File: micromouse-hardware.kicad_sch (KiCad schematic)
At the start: 52 parts, among them Q1 MBT3904DW1, Q2 MBT3904DW1, Q3 MBT3904DW1, Q4 TEFT4300, Q5 TEFT4300, Q6 TEFT4300, Q7 TEFT4300, Q8 TEFT4300, SW1 SLW-116641-5A-S-D, SW2 SW_DIP_x02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

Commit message: before routing
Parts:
- BT1: footprint (none) -> Connector_PinHeader_2.54mm:PinHeader_1x02_P2.54mm_Vertical
- C1, C2, C3, C4, C5: footprint Capacitor_SMD:C_0201_0603Metric -> Capacitor_SMD:C_0603_1608Metric
- L1: value 220uH -> 22uH; footprint Inductor_SMD:L_0201_0603Metric -> Inductor_SMD:L_7.3x7.3_H3.5
- R1, R10, R11, R12, R13, R14, R15, R2, R21, R22, R3, R4, R5, R6, R7, R8, R9: footprint Resistor_SMD:R_0201_0603Metric -> Resistor_SMD:R_0603_1608Metric
- U2: value 74HC4051 -> CD74HC4051NSR; footprint Package_SO:SOIC-14-16_3.9x9.9mm_P1.27mm -> Package_SO:SOIC-16_4.55x10.3mm_P1.27mm
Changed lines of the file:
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@@
 	(label "D11"
 		(at 191.77 203.2 180)
+		(fields_autoplaced yes)
 		(effects
 			(font
@@
 	(label "MUX_SEL_0"
 		(at 95.25 129.54 270)
+		(fields_autoplaced yes)
 		(effects
 			(font
@@
 	(label "D5"
 		(at 190.5 195.58 180)
+		(fields_autoplaced yes)
 		(effects
 			(font
@@
 	(label "A0"
 		(at 261.62 181.61 180)
+		(fields_autoplaced yes)
 		(effects
 			(font
@@
 	(label "D11"
 		(at 90.17 203.2 180)
+		(fields_autoplaced yes)
 		(effects
 			(font
@@
 	(label "IRT_READ"
 		(at 295.91 101.6 180)
+		(fields_autoplaced yes)
 		(effects
 			(font
@@
 	(label "IRT_READ"
 		(at 118.11 190.5 0)
+		(fields_autoplaced yes)
 		(effects
 			(font
@@
 	(label "MUX_SEL_0"
 		(at 300.99 101.6 270)
+		(fields_autoplaced yes)
 		(effects
 			(font
@@
 	(label "D5"
 		(at 88.9 187.96 180)
+		(fields_autoplaced yes)
 		(effects
 			(font
@@
 	(label "A1"
 		(at 261.62 184.15 180)
+		(fields_autoplaced yes)
 		(effects
 			(font
@@
 	(label "D3"
 		(at 190.5 200.66 180)
+		(fields_autoplaced yes)
 		(effects
 			(font
@@
 	(label "D6"
 		(at 88.9 190.5 180)
+		(fields_autoplaced yes)
 		(effects
 			(font
@@
 	(label "A2"
 		(at 261.62 203.2 180)
+		(fields_autoplaced yes)
 		(effects
 			(font
@@
 	(label "MUX_SEL_1"
 		(at 303.53 101.6 270)
+		(fields_autoplaced yes)
 		(effects
 			(font
@@
 	(label "MUX_SEL_0"
 		(at 92.71 185.42 180)
+		(fields_autoplaced yes)
 		(effects
 			(font
@@
 	(label "MUX_SEL_1"
 		(at 97.79 129.54 270)
+		(fields_autoplaced yes)
 		(effects
 			(font
@@
 	(label "MUX_SEL_1"
 		(at 92.71 193.04 180)
+		(fields_autoplaced yes)
 		(effects
 			(font
@@
 	(label "LED_DEMUX_ENABLE"
 		(at 92.71 180.34 180)
+		(fields_autoplaced yes)
 		(effects
 			(font
@@
 	(label "LED_DEMUX_ENABLE"
 		(at 113.03 129.54 0)
+		(fields_autoplaced yes)
 		(effects
 			(font
@@
 	(label "A3"
 		(at 261.62 205.74 180)
+		(fields_autoplaced yes)
 		(effects
 			(font
@@
 	(label "MUX_SEL_2"
 		(at 92.71 195.58 180)
+		(fields_autoplaced yes)
 		(effects
 			(font
@@
 	(label "MUX_SEL_2"
 		(at 100.33 129.54 270)
+		(fields_autoplaced yes)
 		(effects
 			(font
@@
 	(label "D3"
 		(at 88.9 182.88 180)
+		(fields_autoplaced yes)
 		(effects
 			(font
@@
 	(label "D6"
 		(at 190.5 198.12 180)
+		(fields_autoplaced yes)
 		(effects
 			(font
@@
 	(label "MUX_SEL_2"
 		(at 306.07 101.6 270)
+		(fields_autoplaced yes)
 		(effects
 			(font
@@
 			)
 		)
-		(property "Footprint" "Resistor_SMD:R_0201_0603Metric"
+		(property "Footprint" "Resistor_SMD:R_0603_1608Metric"
 			(at 214.122 46.99 90)
 			(effects
@@
 			)
 		)
-		(property "Footprint" "Resistor_SMD:R_0201_0603Metric"
+		(property "Footprint" "Resistor_SMD:R_0603_1608Metric"
 			(at 203.2 61.468 90)
 			(effects
@@
 			)
 		)
-		(property "Footprint" "Resistor_SMD:R_0201_0603Metric"
+		(property "Footprint" "Resistor_SMD:R_0603_1608Metric"
 			(at 85.09 72.898 90)
 			(effects
@@
 			)
 		)
-		(property "Footprint" "Resistor_SMD:R_0201_0603Metric"
+		(property "Footprint" "Resistor_SMD:R_0603_1608Metric"
 			(at 46.99 72.898 90)
 			(effects
@@
 			)
 		)
-		(property "Footprint" "Resistor_SMD:R_0201_0603Metric"
+		(property "Footprint" "Resistor_SMD:R_0603_1608Metric"
 			(at 41.91 61.468 90)
 			(effects
@@
 			)
 		)
-		(property "Value" "74HC4051"
+		(property "Value" "CD74HC4051NSR"
 			(at 287.02 91.0238 90)
 			(effects
@@
 			)
 		)
-		(property "Footprint" "Package_SO:SOIC-14-16_3.9x9.9mm_P1.27mm"
+		(property "Footprint" "Package_SO:SOIC-16_4.55x10.3mm_P1.27mm"
 			(at 313.69 93.98 0)
 			(effects
@@
 			)
 		)
-		(property "Footprint" "Resistor_SMD:R_0201_0603Metric"
+		(property "Footprint" "Resistor_SMD:R_0603_1608Metric"
 			(at 119.38 61.468 90)
 			(effects
@@
 			)
 		)
-		(property "Footprint" ""
+		(property "Footprint" "Connector_PinHeader_2.54mm:PinHeader_1x02_P2.54mm_Vertical"
 			(at 306.07 180.086 90)
 			(effects
@@
 			)
 		)
-		(property "Footprint" "Resistor_SMD:R_0201_0603Metric"
+		(property "Footprint" "Resistor_SMD:R_0603_1608Metric"
 			(at 375.412 181.61 90)
 			(effects
@@
 			)
 		)
-		(property "Footprint" "Capacitor_SMD:C_0201_0603Metric"
+		(property "Footprint" "Capacitor_SMD:C_0603_1608Metric"
 			(at 328.6252 181.61 0)
 			(effects
@@
 			)
 		)
-		(property "Footprint" "Capacitor_SMD:C_0201_0603Metric"
+		(property "Footprint" "Capacitor_SMD:C_0603_1608Metric"
 			(at 390.8552 187.96 0)
 			(effects
@@
 			)
 		)
-		(property "Footprint" "Capacitor_SMD:C_0201_0603Metric"
+		(property "Footprint" "Capacitor_SMD:C_0603_1608Metric"
 			(at 183.8452 180.34 0)
 			(effects
@@
 			)
 		)
-		(property "Footprint" "Resistor_SMD:R_0201_0603Metric"
+		(property "Footprint" "Resistor_SMD:R_0603_1608Metric"
 			(at 124.46 72.898 90)
 			(effects
@@
 			)
 		)
-		(property "Footprint" "Resistor_SMD:R_0201_0603Metric"
+		(property "Footprint" "Resistor_SMD:R_0603_1608Metric"
 			(at 208.28 72.898 90)
 			(effects
@@
 			)
 		)
-		(property "Value" "220uH"
+		(property "Value" "22uH"
 			(at 351.79 171.45 90)
 			(effects
@@
 			)
 		)
-		(property "Footprint" "Inductor_SMD:L_0201_0603Metric"
+		(property "Footprint" "Inductor_SMD:L_7.3x7.3_H3.5"
 			(at 351.79 173.99 0)
 			(effects
@@
 			)
 		)
-		(property "Description" "Inductor"
+		(property "Description" "IFDC3030EZER220M"
 			(at 351.79 173.99 0)
 			(effects
@@
 			)
 		)
-		(property "Footprint" "Capacitor_SMD:C_0201_0603Metric"
+		(property "Footprint" "Capacitor_SMD:C_0603_1608Metric"
 			(at 224.4852 179.07 0)
 			(effects
@@
 			)
 		)
-		(property "Footprint" "Resistor_SMD:R_0201_0603Metric"
+		(property "Footprint" "Resistor_SMD:R_0603_1608Metric"
 			(at 168.402 46.99 90)
 			(effects
@@
 			)
 		)
-		(property "Footprint" "Resistor_SMD:R_0201_0603Metric"
+		(property "Footprint" "Resistor_SMD:R_0603_1608Metric"
 			(at 157.48 61.468 90)
 			(effects
@@
 			)
 		)
-		(property "Footprint" "Resistor_SMD:R_0201_0603Metric"
+		(property "Footprint" "Resistor_SMD:R_0603_1608Metric"
 			(at 80.01 61.468 90)
 			(effects
@@
 			)
 		)
-		(property "Footprint" "Resistor_SMD:R_0201_0603Metric"
+		(property "Footprint" "Resistor_SMD:R_0603_1608Metric"
 			(at 52.832 46.99 90)
 			(effects
@@
 			)
 		)
-		(property "Footprint" "Resistor_SMD:R_0201_0603Metric"
+		(property "Footprint" "Resistor_SMD:R_0603_1608Metric"
 			(at 90.932 46.99 90)
 			(effects
@@
 			)
 		)
-		(property "Footprint" "Capacitor_SMD:C_0201_0603Metric"
+		(property "Footprint" "Capacitor_SMD:C_0603_1608Metric"
 			(at 233.3752 179.07 0)
 			(effects
@@
 			)
 		)
-		(property "Footprint" "Resistor_SMD:R_0201_0603Metric"
+		(property "Footprint" "Resistor_SMD:R_0603_1608Metric"
 			(at 162.56 72.898 90)
 			(effects
@@
 			)
 		)
-		(property "Footprint" "Resistor_SMD:R_0201_0603Metric"
+		(property "Footprint" "Resistor_SMD:R_0603_1608Metric"
 			(at 130.302 46.99 90)
 			(effects
@@
 			)
 		)
-		(property "Footprint" "Resistor_SMD:R_0201_0603Metric"
+		(property "Footprint" "Resistor_SMD:R_0603_1608Metric"
 			(at 375.412 195.58 90)
 			(effects

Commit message: nesto stabilno
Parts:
- added R23, R24: 10K, Resistor_SMD:R_0603_1608Metric, symbol Device:R
- D6: footprint Diode_SMD:D_0201_0603Metric -> Diode_SMD:D_0603_1608Metric_Pad1.05x0.95mm_HandSolder
- U2: value CD74HC4051NSR -> CD74HC4051M
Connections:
- net GND: now also R23.1, R24.1
- net at A1.15 (D12), SW2.2: now also R24.2
- net at A1.16 (D13), SW2.1: now also R23.2

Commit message: before arduino rotae
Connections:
- net A0 is gone; now on net A1: ME1.3 (C1)
- net A1: now also A1.20 (A1); no longer ME1.4 (C2)
- net A2: now also A1.21 (A2), ME1.4 (C2); no longer ME2.3 (C1)
- net A3: now also A1.22 (A3)
- net A4: now reaches A1.23 (A4)
- net A4: now also ME2.3 (C1)
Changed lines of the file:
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@@
+	(wire
+		(pts
+			(xy 259.08 203.2) (xy 261.62 203.2)
+		)
+		(stroke
+			(width 0)
+			(type default)
+		)
+	)
 	(wire
 		(pts
@@
 		(pts
 			(xy 88.9 71.12) (xy 92.71 71.12)
+		)
+		(stroke
+			(width 0)
+			(type default)
+		)
+	)
+	(wire
+		(pts
+			(xy 259.08 205.74) (xy 261.62 205.74)
 		)
 		(stroke
@@
 		)
 	)
-	(label "A0"
+	(label "A3"
+		(at 118.11 198.12 0)
+		(effects
+			(font
+				(size 1.27 1.27)
+			)
+			(justify left bottom)
+		)
+	)
+	(label "A1"
 		(at 261.62 181.61 180)
 		(effects
@@
 		)
 	)
-	(label "A1"
+	(label "A4"
+		(at 259.08 203.2 0)
+		(effects
+			(font
+				(size 1.27 1.27)
+			)
+			(justify left bottom)
+		)
+	)
+	(label "A2"
 		(at 261.62 184.15 180)
 		(effects
@@
 			)
 			(justify right bottom)
+		)
+	)
+	(label "A2"
+		(at 118.11 195.58 0)
+		(effects
+			(font
+				(size 1.27 1.27)
+			)
+			(justify left bottom)
 		)
 	)
@@
 		)
 	)
-	(label "A2"
-		(at 261.62 203.2 180)
-		(effects
-			(font
-				(size 1.27 1.27)
-			)
-			(justify right bottom)
-		)
-	)
 	(label "MUX_SEL_1"
 		(at 303.53 101.6 270)
@@
 		)
 	)
-	(label "A3"
-		(at 261.62 205.74 180)
-		(effects
-			(font
-				(size 1.27 1.27)
-			)
-			(justify right bottom)
+	(label "A4"
+		(at 118.11 200.66 0)
+		(effects
+			(font
+				(size 1.27 1.27)
+			)
+			(justify left bottom)
+		)
+	)
+	(label "A1"
+		(at 118.11 193.04 0)
+		(effects
+			(font
+				(size 1.27 1.27)
+			)
+			(justify left bottom)
 		)
 	)
@@
 		)
 	)
+	(label "A3"
+		(at 259.08 205.74 0)
+		(effects
+			(font
+				(size 1.27 1.27)
+			)
+			(justify left bottom)
+		)
+	)

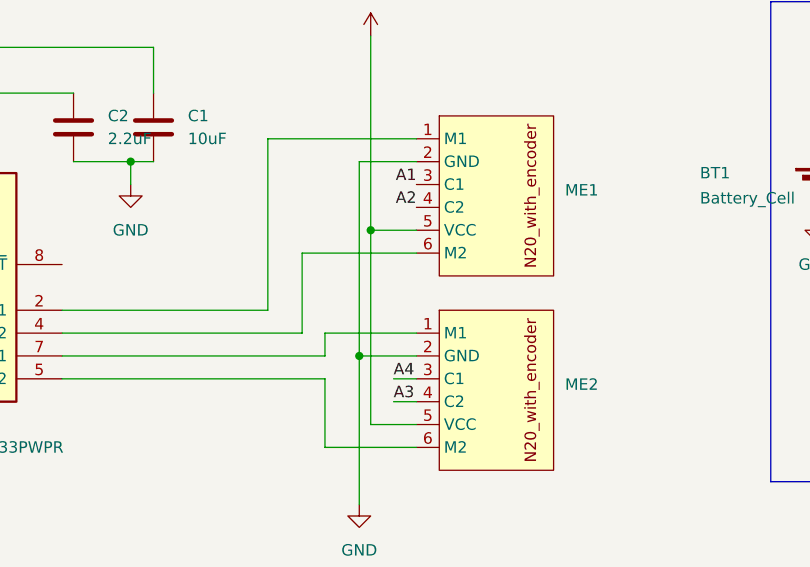
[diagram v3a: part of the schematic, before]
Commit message: everything except ground plane
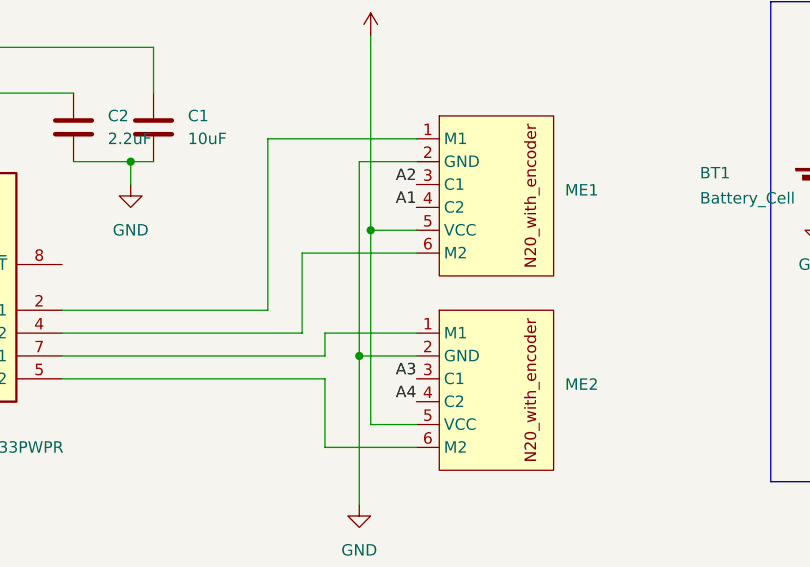
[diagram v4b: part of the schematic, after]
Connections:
- net A1: now also ME1.4 (C2); no longer ME1.3 (C1)
- net A2: now also ME1.3 (C1); no longer ME1.4 (C2)
- net A3: now also ME2.3 (C1); no longer ME2.4 (C2)
- net A4: now also ME2.4 (C2); no longer ME2.3 (C1)
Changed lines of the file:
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@@
-	(wire
-		(pts
-			(xy 259.08 203.2) (xy 261.62 203.2)
-		)
-		(stroke
-			(width 0)
-			(type default)
-		)
-	)
 	(wire
 		(pts
@@
 		(pts
 			(xy 88.9 71.12) (xy 92.71 71.12)
-		)
-		(stroke
-			(width 0)
-			(type default)
-		)
-	)
-	(wire
-		(pts
-			(xy 259.08 205.74) (xy 261.62 205.74)
 		)
 		(stroke
@@
 	)
 	(label "A1"
-		(at 261.62 181.61 180)
+		(at 261.62 184.15 180)
 		(effects
 			(font
@@
 		)
 	)
-	(label "A4"
-		(at 259.08 203.2 0)
-		(effects
-			(font
-				(size 1.27 1.27)
-			)
-			(justify left bottom)
-		)
-	)
 	(label "A2"
-		(at 261.62 184.15 180)
+		(at 261.62 181.61 180)
 		(effects
 			(font
@@
 		)
 	)
+	(label "A3"
+		(at 261.62 203.2 180)
+		(effects
+			(font
+				(size 1.27 1.27)
+			)
+			(justify right bottom)
+		)
+	)
 	(label "MUX_SEL_1"
 		(at 303.53 101.6 270)
@@
 		)
 	)
+	(label "A4"
+		(at 261.62 205.74 180)
+		(effects
+			(font
+				(size 1.27 1.27)
+			)
+			(justify right bottom)
+		)
+	)
 	(label "MUX_SEL_2"
 		(at 92.71 195.58 180)
@@
 		)
 	)
-	(label "A3"
-		(at 259.08 205.74 0)
-		(effects
-			(font
-				(size 1.27 1.27)
-			)
-			(justify left bottom)
-		)
-	)

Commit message: limit
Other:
- note added: "5V regulator - peak ~1A i const ~300mA"
- note removed: "5V regulator"
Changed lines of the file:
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@@
 		)
 	)
-	(text "5V regulator"
+	(text "5V regulator - peak ~1A i const ~300mA"
 		(exclude_from_sim no)
-		(at 307.848 159.258 0)
+		(at 321.31 159.004 0)
 		(effects
 			(font

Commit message: Arduino Nano - Regulated 5V should be connected to 5V not VIN Moved some labels around to make connections more visible Placed No Connect Flags on all unused pins Added descriptive names to labels Changed the 5V regulator to LM2575GR-5.0 Made the Motor Driver use the battery voltage directly Re-routed some parts of the PCB to make space
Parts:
- removed D6: SS34, Diode_SMD:D_0603_1608Metric_Pad1.05x0.95mm_HandSolder, symbol Device:D_Schottky
- removed R21: 110K, Resistor_SMD:R_0603_1608Metric, symbol Device:R
- removed R22: 15K, Resistor_SMD:R_0603_1608Metric, symbol Device:R
- removed SW1: SLW-116641-5A-S-D, Connector_PinHeader_2.54mm:PinHeader_1x03_P2.54mm_Vertical, symbol Switch:SW_SPDT
- removed U4: MT3608, Package_TO_SOT_SMD:SOT-23-6, symbol Regulator_Switching:MT3608
- added BT2: Battery_Cell, Connector_PinHeader_2.54mm:PinHeader_1x02_P2.54mm_Vertical, symbol Device:Battery_Cell
- added C6: 470uF, Capacitor_SMD:C_Elec_8x10.2, symbol Device:C
- added C7: 100nF, Capacitor_SMD:C_0603_1608Metric, symbol Device:C
- added D8: SS26, Diode_SMD:D_SMA, symbol Diode:SS26
- added J1: BATT-CONN, Connector_PinHeader_2.54mm:PinHeader_1x02_P2.54mm_Vertical, symbol Connector_Generic:Conn_01x02
- added unit 2 of Q3
- added SW3: SLW-116641-5A-S-D, Connector_PinHeader_2.54mm:PinHeader_1x03_P2.54mm_Vertical, symbol Switch:SW_SPDT
- added U5: LM2575GR-5.0, Package_TO_SOT_SMD:TO-263-5_TabPin3, symbol Regulator_Switching:LM2575-5.0BU
- BT1: now left out of the parts list
- C4: value 22uF X7R -> 470uF; footprint Capacitor_SMD:C_0603_1608Metric -> Capacitor_SMD:C_Elec_8x10.2; Order Link (none) -> https://www.tme.eu/en/details/sc1c477m08010vr/smd-electroly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
- C5: value 22uF X7R -> 100nF; Order Link (none) -> https://www.tme.eu/en/details/cl10b104kb8nnnc/mlcc-smd-capa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
- L1: value 22uH -> 220uH; footprint Inductor_SMD:L_7.3x7.3_H3.5 -> Inductor_SMD:L_12x12mm_H8mm; Order Link (none) -> https://www.tme.eu/en/details/pcs129mt221/inductors/viking/
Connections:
- net +5V: now also A1.27 (+5V), C4.1, L1.2, C7.1, U5.4 (FB); no longer A1.30 (VIN), C1.1, C3.1, C5.1, U1.12 (VM)
- net GND: now also BT2.2 (-), C6.2, C7.2, D8.2 (A), J1.1 (Pin_1), Q3.3 (C2), Q3.4 (E2), Q3.5 (B2), U5.3 (GND), U5.5 (~{ON}/OFF); no longer BT1.2 (-)
- net at L1.1: now also D8.1 (K), U5.2 (OUT); no longer C4.1
- net at BT1.1 (+): now also J1.2 (Pin_2), SW3.2 (B)
- net A1 renamed M1-C1
- net M1-C1: now also ME1.3 (C1); no longer ME1.4 (C2)
- net A2 renamed M1-C2
- net M1-C2: now also ME1.4 (C2); no longer ME1.3 (C1)
- net A3 renamed M2-C1
- net M2-C1: now also A1.23 (A4); no longer A1.22 (A3)
- net A4 renamed M2-C2
- net M2-C2: now also A1.22 (A3); no longer A1.23 (A4)
- net D11 renamed M2-IN2
- net D3 renamed M2-IN1
- net D5 renamed M1-IN1
- net D6 renamed M1-IN2
- new net: BT1.2 (-), BT2.1 (+)
- new net +VBAT: C1.1, C3.1, C5.1, C6.1, SW3.1 (A), U1.12 (VM), U5.1 (VIN)
- no-connect marks 0 -> 20
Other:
- moved on the sheet: C3, ME1, ME2, R24

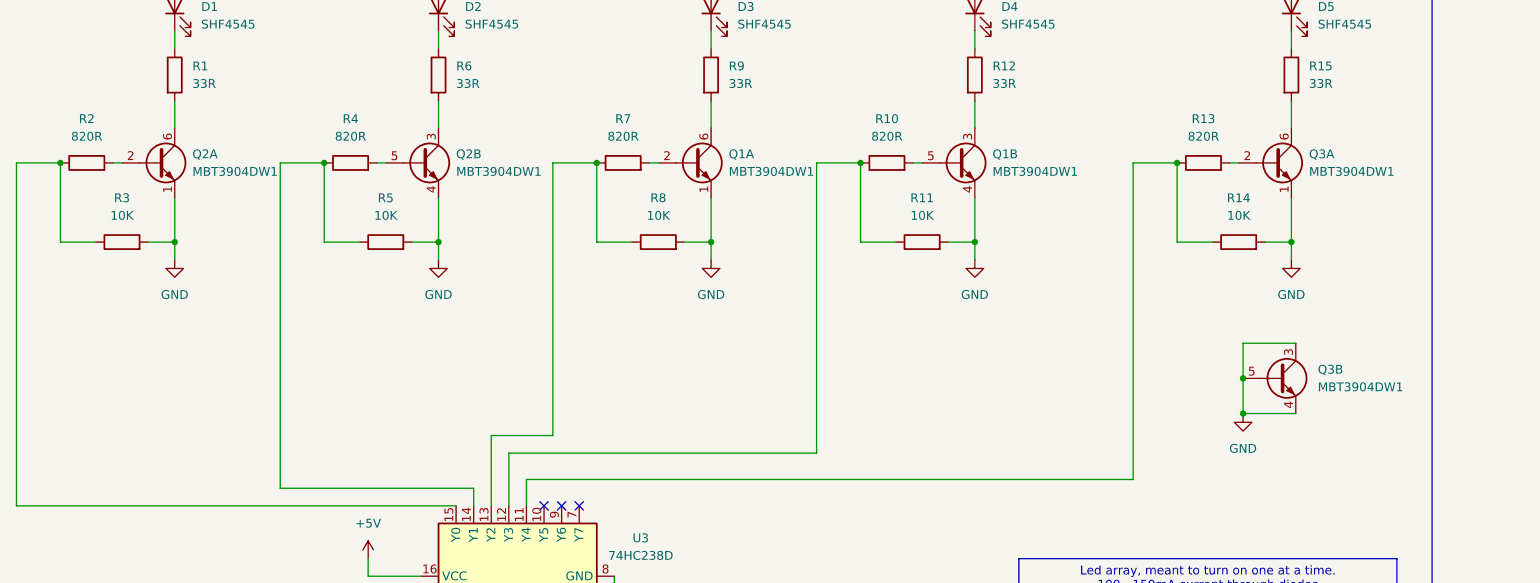
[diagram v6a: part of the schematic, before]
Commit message: Change the transistor footprint, changed spacing around the components to allow for mounting hardware to be added
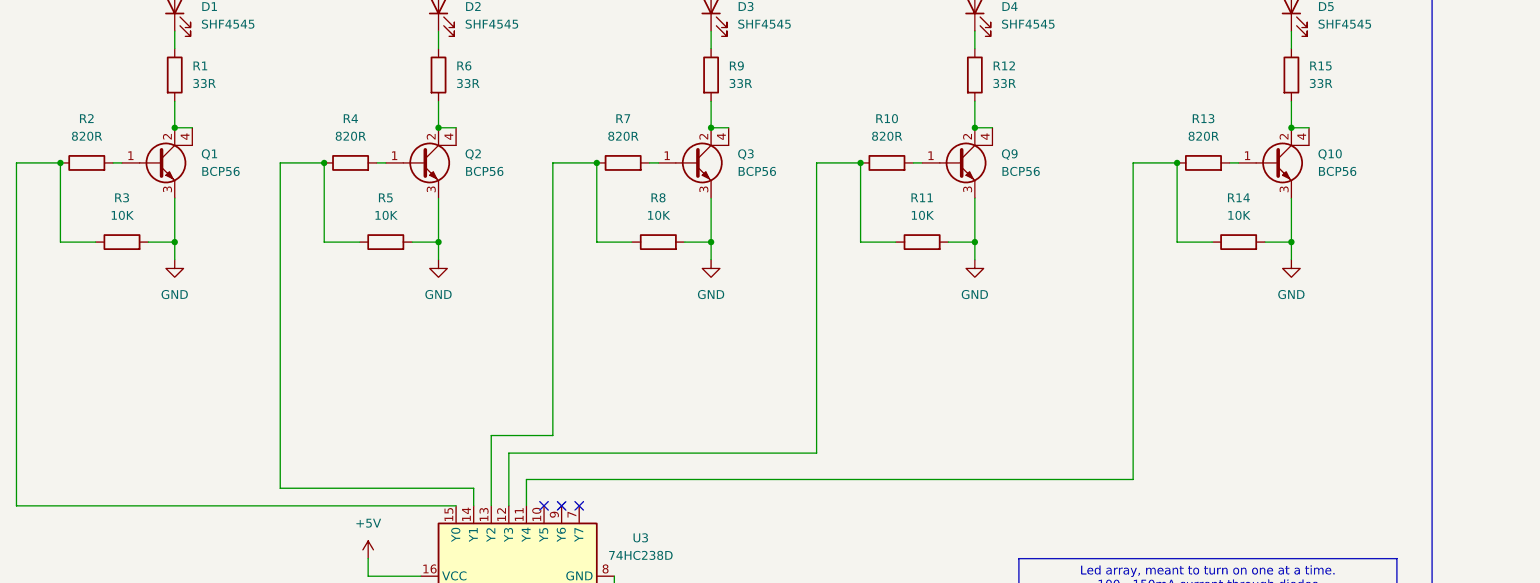
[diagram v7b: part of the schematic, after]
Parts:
- removed Q1, Q2, Q3: MBT3904DW1, Package_TO_SOT_SMD:SOT-363_SC-70-6, symbol Transistor_BJT:MBT3904DW1
- added Q1, Q10, Q2, Q3, Q9: BCP56, Custom:SOT-223-3_TabPin4, symbol Transistor_BJT:BCP56
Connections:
- net GND: now also Q1.3 (E), Q10.3 (E), Q2.3 (E), Q3.3 (E), Q9.3 (E)
- net at R15.2: now also Q10.2 (C), Q10.4 (C)
- net at R6.2: now also Q2.2 (C), Q2.4 (C)
- net at R4.2: now also Q2.1 (B)
- net at R13.2: now also Q10.1 (B)
- net at R12.2: now also Q9.2 (C), Q9.4 (C)
- net at R10.2: now also Q9.1 (B)
- net at R2.2: now also Q1.1 (B)
- net at R7.2: now also Q3.1 (B)
- net at R9.2: now also Q3.2 (C), Q3.4 (C)
- net at R1.2: now also Q1.2 (C), Q1.4 (C)
